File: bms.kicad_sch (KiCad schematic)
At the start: 24 parts, among them Q1 DUAL_N_FET, U1 BQ7692003

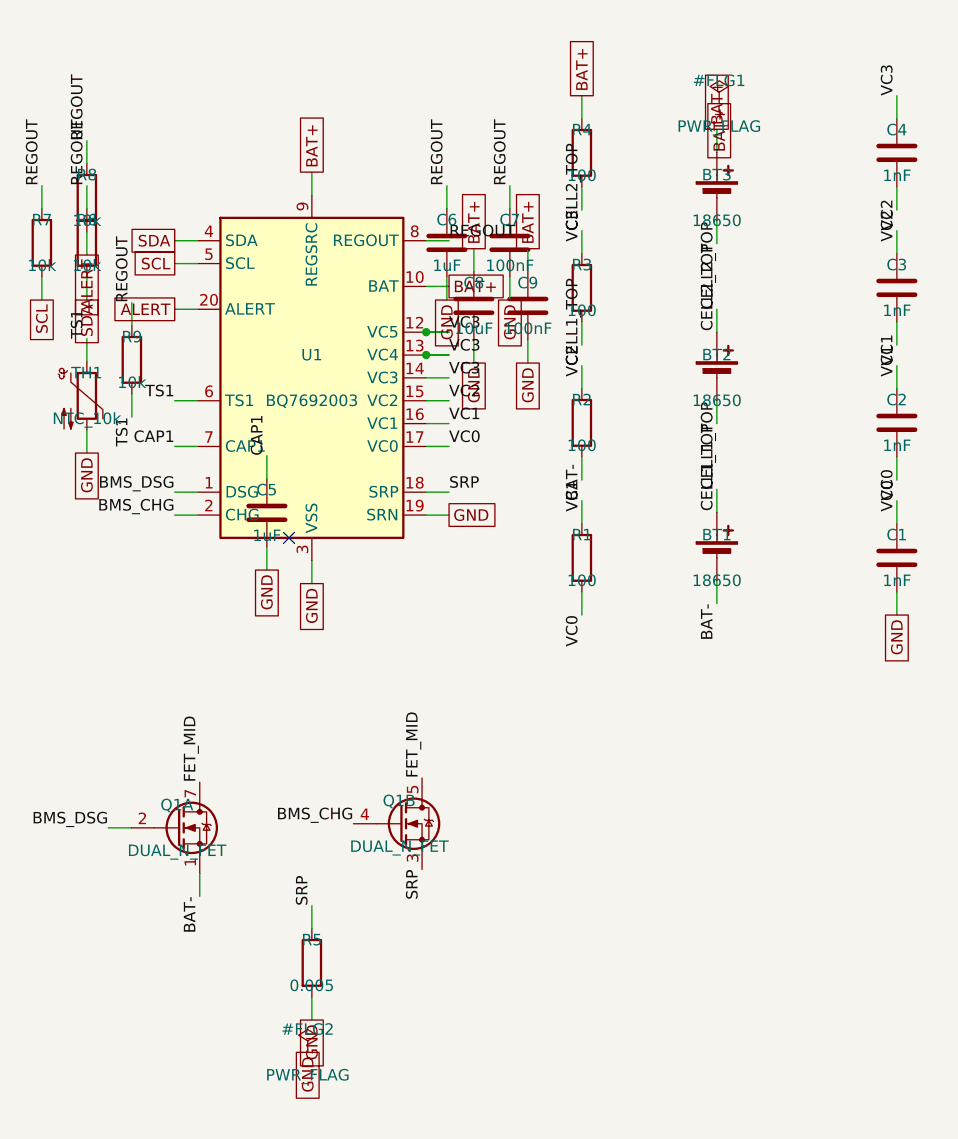
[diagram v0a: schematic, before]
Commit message: schematic: parts pass + cell-holder and USB-C symbol swaps
- Apply Footprint + LCSC + Description to all 67 non-cell components
  across bms / charger / buckboost (JLCPCB-friendly BOM).
- Add project-local power_module_lib (symbols + footprints fetched via
  easyeda2kicad for BH-18650-B5BA016 holder and the two custom-package
  inductors).
- bms: replace BT1-3 (3x Battery_Cell) with single 6-pin BAT1 holder
  (BH-18650-B5BA016, C19184086). Pin mapping respects all-cells-same-
  direction; CELL1_TOP/CELL2_TOP taps repeat on inner pins.
- charger: swap J1 from USB_C_Receptacle_PowerOnly_24P to
  USB_C_Receptacle_USB2.0_16P (matches HRO TYPE-C-31-M-12 16P
  footprint). NC the 6 unused USB 2.0 data + SBU pins.
- R21 value 90k -> 91k (E96 standard so 0603 1% available at JLC).
- ERC on charger dropped 9 -> 2 (remaining: pre-existing Input Power
  flag, plus harmless 'fp-lib-table missing' warning resolved at
  project scope).

Co-Authored-By: Claude Opus 4.7 <noreply@anthropic.com>
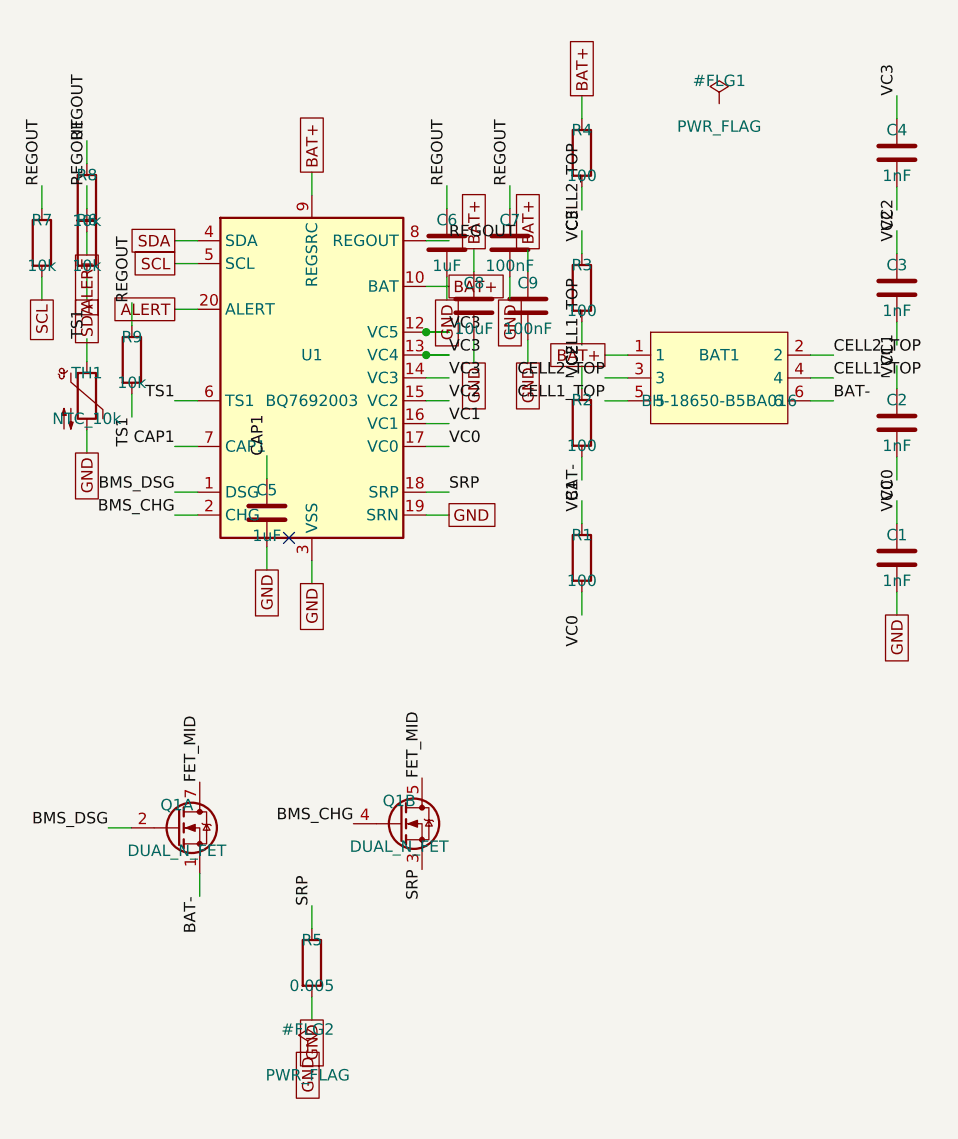
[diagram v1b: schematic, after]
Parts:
- removed BT1, BT2, BT3: 18650, symbol Device:Battery_Cell
- added BAT1: BH-18650-B5BA016, power_module_lib:BAT-SMD_BH-18650-B5BA016, symbol power_module_lib:BH-18650-B5BA016
- C1, C2, C3, C4: footprint (none) -> Capacitor_SMD:C_0603_1608Metric; LCSC (none) -> C1588
- C5, C6: footprint (none) -> Capacitor_SMD:C_0805_2012Metric; LCSC (none) -> C28323
- C7, C9: footprint (none) -> Capacitor_SMD:C_0603_1608Metric; LCSC (none) -> C14663
- C8: footprint (none) -> Capacitor_SMD:C_0805_2012Metric; LCSC (none) -> C15850
- Q1: footprint (none) -> Package_SO:SOIC-8_3.9x4.9mm_P1.27mm; LCSC (none) -> C353066
- R1, R2, R3, R4: footprint (none) -> Resistor_SMD:R_0603_1608Metric; LCSC (none) -> C22775
- R5: footprint (none) -> Resistor_SMD:R_1206_3216Metric; LCSC (none) -> C2988648
- R6, R7, R8, R9: footprint (none) -> Resistor_SMD:R_0603_1608Metric; LCSC (none) -> C25804
- TH1: footprint (none) -> Resistor_SMD:R_0603_1608Metric; LCSC (none) -> C13564
- U1: LCSC (none) -> C601650
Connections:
- net BAT+: now also BAT1.1
- net BAT-: now also BAT1.6
- net CELL1_TOP: now also BAT1.4, BAT1.5
- net CELL2_TOP: now also BAT1.2, BAT1.3

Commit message: power_module: Placement_Anchor on C9, mcp_constraint_version=1
First use of the new placement-constraint v1 tooling. C9 (100 nF
decoupling for U1's BAT pin) now carries
`Placement_Anchor = "U1.9/within=3mm"` on bms.kicad_sch — the
audit/place_near tools honor this as an explicit anchor.

PCB position unchanged this commit; the actual move + reroute is a
follow-up (`place_near` works but stripped C9's BAT+/GND routing,
took DRC from 0→5 errors — see NOTES.md for the dance to do it
cleanly).

Co-Authored-By: Claude Opus 4.7 <noreply@anthropic.com>
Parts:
- C9: Placement_Anchor (none) -> U1.9/within=3mm
